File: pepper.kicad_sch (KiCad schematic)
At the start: 48 parts, among them J1 USB, J2 Debug, Q1 BSS138, SW1 Reset, SW2 Boot, SW3 Action, U1 ESP32-S3-WROOM-1, U2 AP2112K-3.3

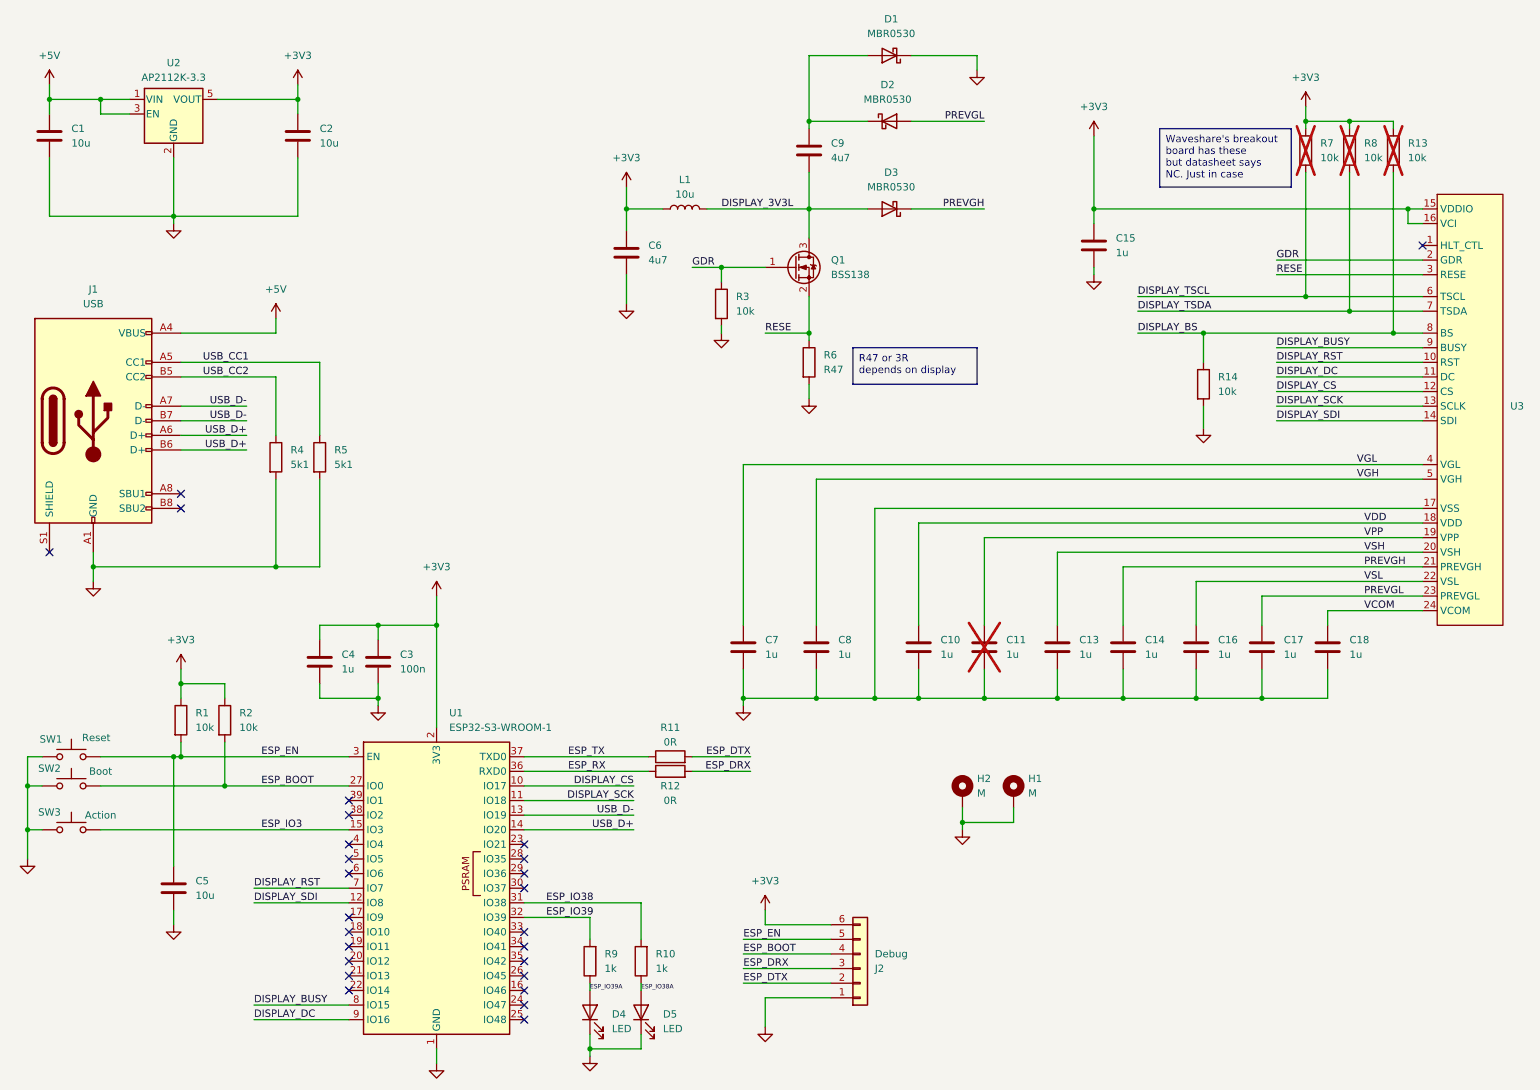
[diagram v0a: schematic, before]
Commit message: Redesign. Bottom control panel
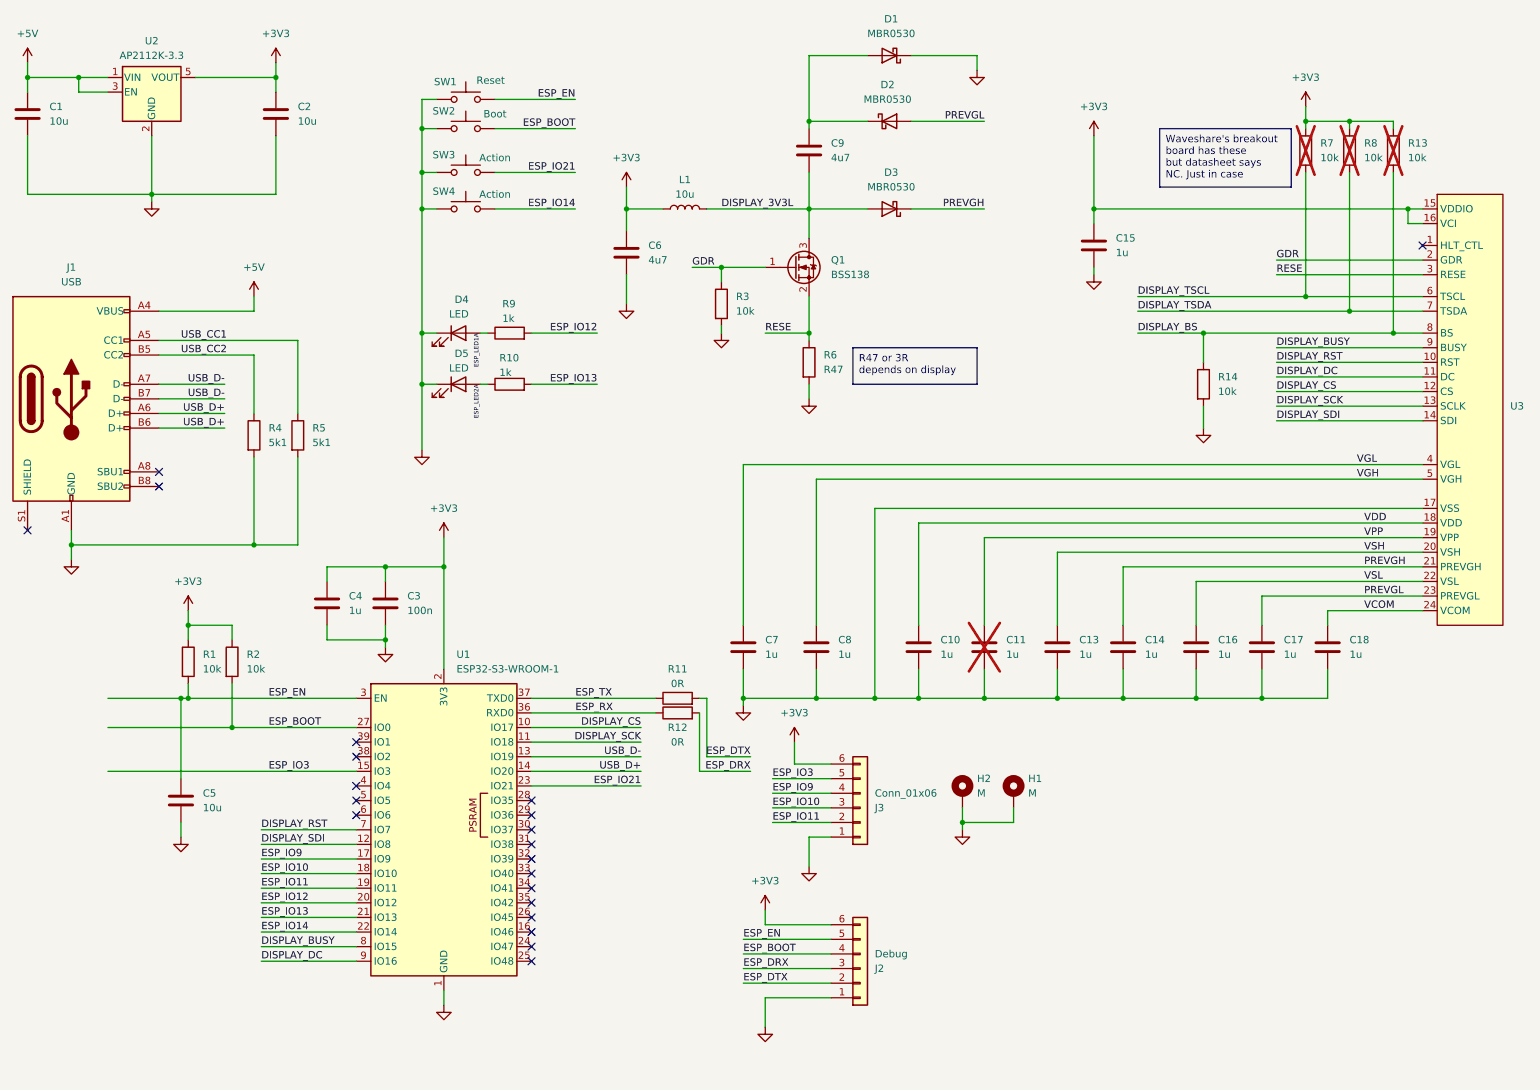
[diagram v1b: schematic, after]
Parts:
- added J3: Conn_01x06, Connector_PinHeader_2.54mm:PinHeader_1x06_P2.54mm_Horizontal, symbol Connector_Generic:Conn_01x06
- added SW4: Action, Button_Switch_SMD:SW_SPST_B3U-1000P, symbol Switch:SW_Push
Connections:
- net +3V3: now also J3.6 (Pin_6)
- net ESP_IO3: now also J3.5 (Pin_5); no longer SW3.2
- net GND: now also J3.1 (Pin_1), SW4.1
- net ESP_IO9: now reaches U1.17 (IO9)
- net ESP_IO9: now also J3.4 (Pin_4)
- net ESP_IO10: now reaches U1.18 (IO10)
- net ESP_IO10: now also J3.3 (Pin_3)
- net ESP_IO11: now reaches U1.19 (IO11)
- net ESP_IO11: now also J3.2 (Pin_2)
- net ESP_IO12: now reaches U1.20 (IO12)
- net ESP_IO12: now also R9.2
- net ESP_IO13: now reaches U1.21 (IO13)
- net ESP_IO13: now also R10.2
- net ESP_IO14: now reaches U1.22 (IO14)
- net ESP_IO14: now also SW4.2
- net ESP_IO21: now reaches U1.23 (IO21)
- net ESP_IO21: now also SW3.2
- net ESP_IO38: no longer names the net of U1.31 (IO38)
- net ESP_IO38: no longer R10.2
- net ESP_IO38A renamed ESP_LED2A
- net ESP_IO39: no longer names the net of U1.32 (IO39)
- net ESP_IO39: no longer R9.2
- net ESP_IO39A renamed ESP_LED1A
- no-connect marks 26 -> 21
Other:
- moved on the sheet: C1, C2, C3, C4, C5, J1, R1, R11, R12, R2, R4, R5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

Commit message: 4 layer board. Battery charger
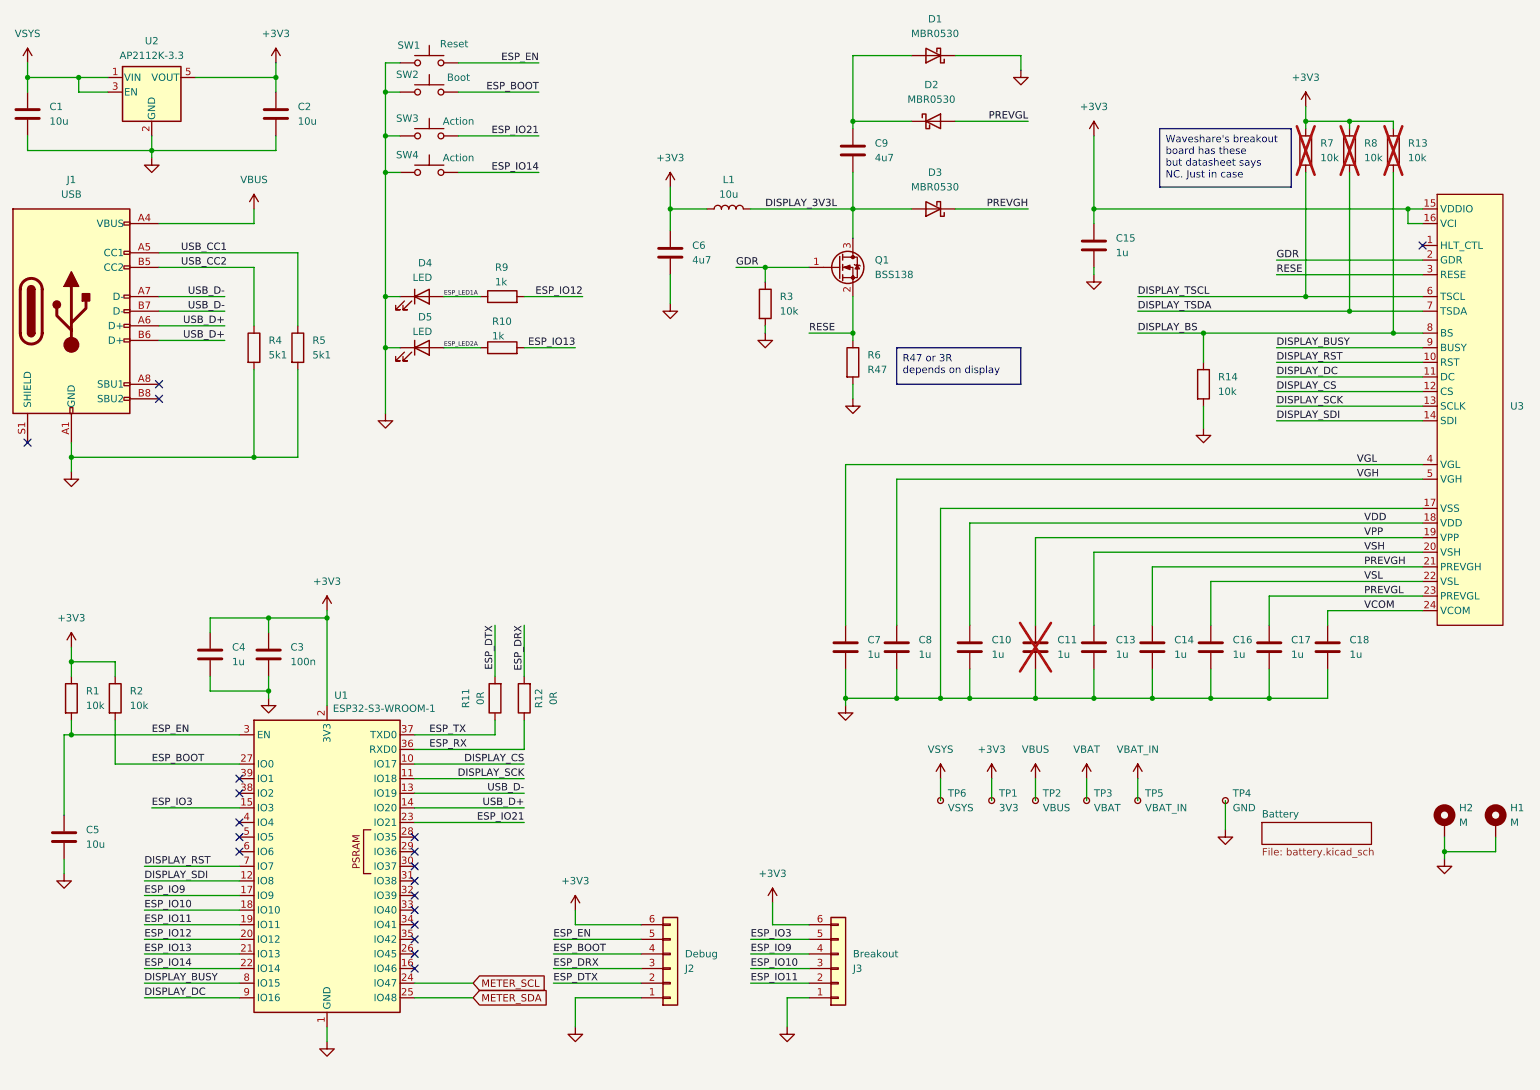
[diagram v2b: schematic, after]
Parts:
- added TP1: 3V3, TestPoint:TestPoint_Pad_D1.0mm, symbol Connector:TestPoint_Small
- added TP2: VBUS, TestPoint:TestPoint_Pad_D1.0mm, symbol Connector:TestPoint_Small
- added TP3: VBAT, TestPoint:TestPoint_Pad_D1.0mm, symbol Connector:TestPoint_Small
- added TP4: GND, TestPoint:TestPoint_Pad_D1.0mm, symbol Connector:TestPoint_Small
- added TP5: VBAT_IN, TestPoint:TestPoint_Pad_D1.0mm, symbol Connector:TestPoint_Small
- added TP6: VSYS, TestPoint:TestPoint_Pad_D1.0mm, symbol Connector:TestPoint_Small
- J3: value Conn_01x06 -> Breakout
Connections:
- net +3V3: now also TP1.1
- net GND: now also TP4.1
- net METER_SCL: now reaches U1.24 (IO47)
- net METER_SDA: now reaches U1.25 (IO48)
- net +5V renamed VBUS
- net VBUS: now also TP2.1; no longer C1.1, U2.1 (VIN), U2.3 (EN)
- new net VBAT: TP3.1
- new net VBAT_IN: TP5.1
- new net VSYS: C1.1, TP6.1, U2.1 (VIN), U2.3 (EN)
- no-connect marks 21 -> 19
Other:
- added sheet Battery (battery.kicad_sch)
- moved on the sheet: C10, C11, C13, C14, C16, C17, C3, C4, C5, C6, C7, C8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
